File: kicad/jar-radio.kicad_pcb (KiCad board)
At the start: 2 copper layers, 84 x 84 mm, 68 parts, among them J1 USB-C 5V, J2 BATT PH2.0, J3 ANT wire, J4 SPEAKER, Q1 AO3401A, U1 Si4825-A10, U2 NS8002, U3 TP4056, U4 XC6206P332MR, U5 XC61CN2702MR, U6 XB8089D, Y1 32.768kHz

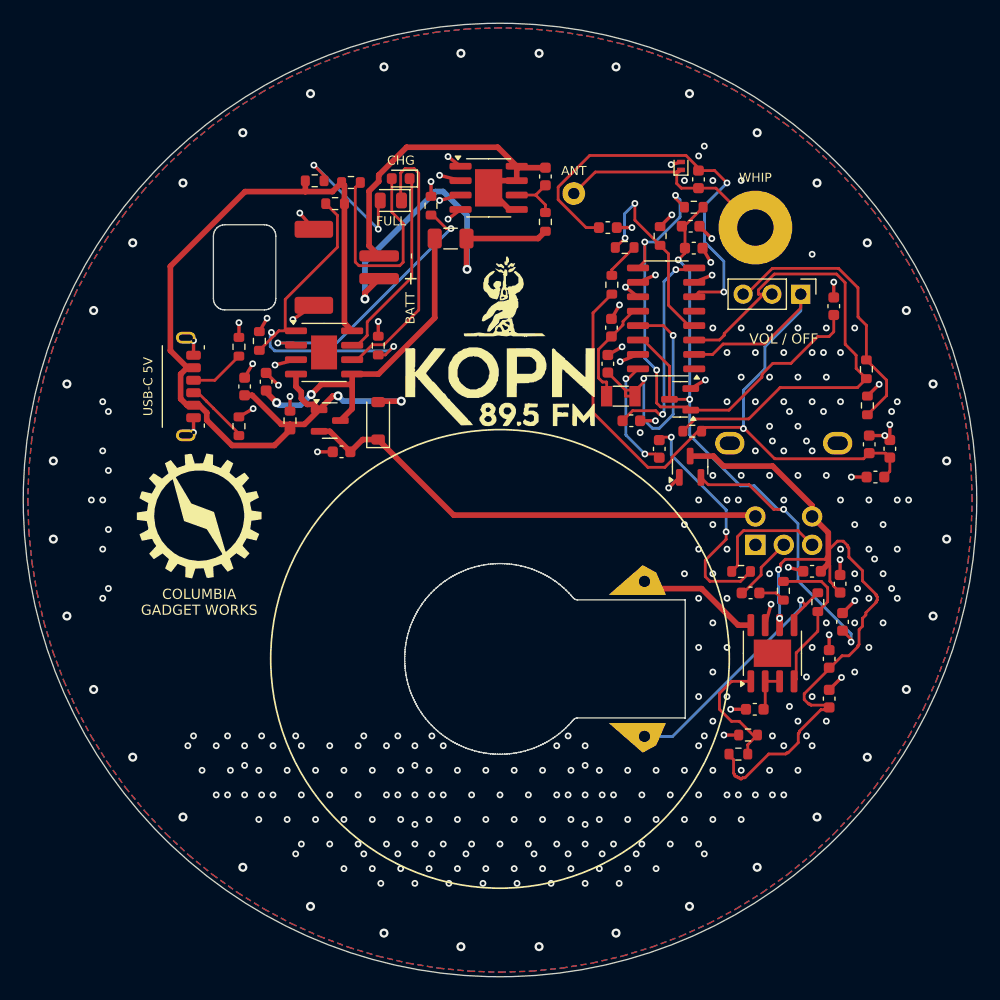
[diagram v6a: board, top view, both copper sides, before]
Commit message: Route with polarity jumpers, moved antenna hole and speaker labels (0 unconnected); exports, renders, BOM check and plan regenerated
Co-Authored-By: Claude Opus 5.5 <noreply@anthropic.com>
Claude-Session: https://claude.ai/code/session_01UChZ4MGw6SzykNSB399iC4
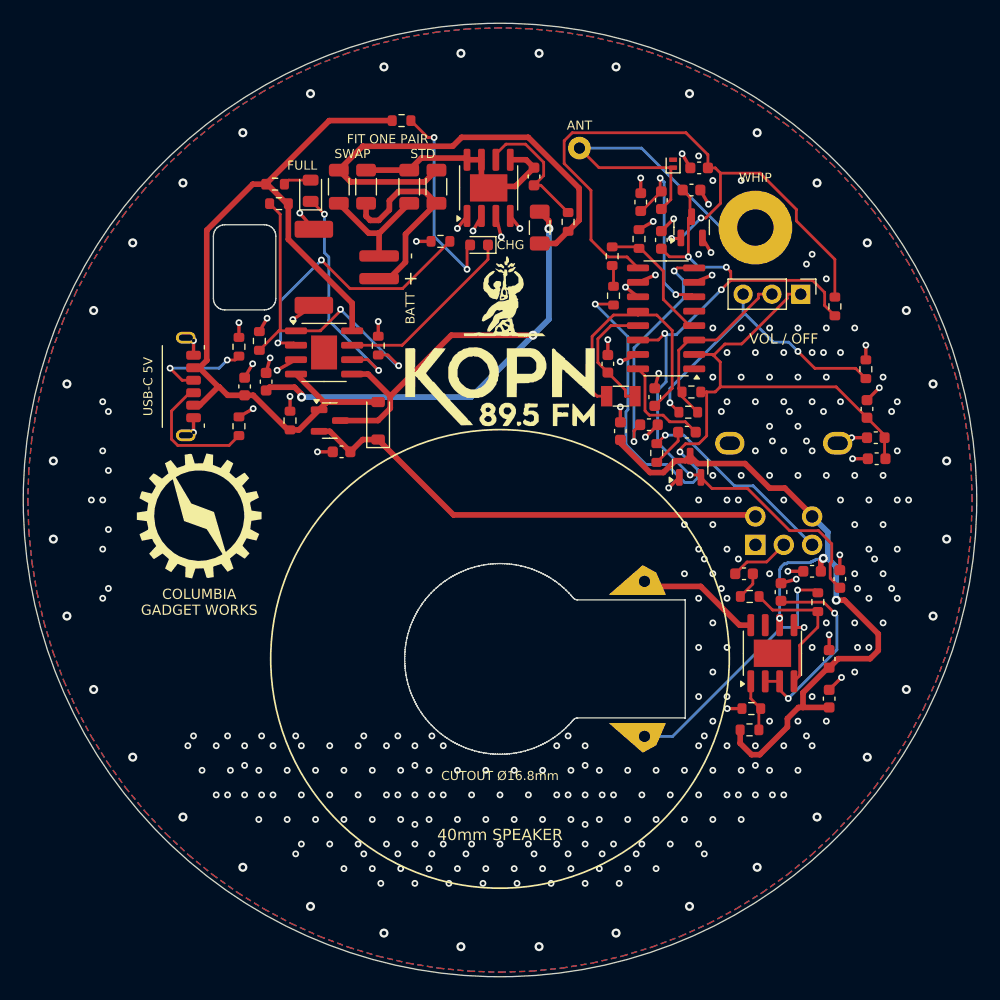
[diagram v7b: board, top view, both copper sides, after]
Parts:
- added R23: 0R (pin1 = -), Resistor_SMD:R_1206_3216Metric, F.Cu at (142.0, 72.4)
- added R24: 0R (pin2 = +), Resistor_SMD:R_1206_3216Metric, F.Cu at (144.4, 72.4)
- added R25: 0R (DNP, pin1 = +), Resistor_SMD:R_1206_3216Metric, F.Cu at (135.8, 72.4)
- added R26: 0R (DNP, pin2 = -), Resistor_SMD:R_1206_3216Metric, F.Cu at (138.2, 72.4)
- moved C19 23.6 mm to (160.6, 93.9)
- moved C5 17.0 mm to (167.5, 70.7), turned to 180 degrees
- moved R3 16.1 mm to (166.6, 92.3), turned to 180 degrees
- moved R1 15.2 mm to (179.5, 82.9), turned to 90 degrees
- moved U5 15.2 mm to (166.9, 76.0), turned to 90 degrees
- moved R22 12.8 mm to (163.8, 95.9), turned to 90 degrees
- moved C12 10.6 mm to (174.8, 108.1), turned to 90 degrees
- moved D2 9.05 mm to (148.2, 77.5)
- moved F1 7.91 mm to (153.5, 76.0), turned to 90 degrees
- moved C2 7.21 mm to (163.6, 90.9)
- moved D3 7.12 mm to (133.3, 72.8), turned to 90 degrees
- moved R14 7.04 mm to (141.3, 66.6)
- moved R20 4.94 mm to (130.5, 73.9)
- moved J3 4.03 mm to (157.0, 69.0)
- moved C20 3.79 mm to (179.9, 107.0)
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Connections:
- J2 pad 1: BAT_N -> BATJ1
- J2 pad 2: BAT_P -> BATJ2
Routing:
- net VBAT: track 29.8 -> 63.1 mm, vias 2 -> 3
- net TUNE2: track 45.4 -> 16.6 mm
- net FMI: track 36.8 -> 16.3 mm
- net BATJ2: track 0.00 -> 18.7 mm
- net AOUT_C: track 20.7 -> 3.44 mm, vias 2 -> 0
- net AMP_BYP: track 3.79 -> 17.6 mm, vias 0 -> 2
- net XTALO: track 9.68 -> 22.3 mm
- net RST: track 45.0 -> 57.3 mm, vias 3 -> 2
- net XTALI: track 23.3 -> 10.9 mm, vias 2 -> 0
- net ANT: track 19.9 -> 31.4 mm
- net BAT_N: track 31.5 -> 20.5 mm
- net BATJ1: track 0.00 -> 10.4 mm
- net LEDG_A: track 12.4 -> 2.46 mm, vias 2 -> 0
- net BAT_P: track 32.7 -> 40.8 mm, vias 2 -> 0
- net VOL_TOP: track 10.6 -> 18.0 mm, vias 0 -> 1
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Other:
- board text added: "40mm SPEAKER"
- board text added: "CUTOUT Ø16.8mm"
- board text added: "FIT ONE PAIR"
- board text added: "STD"
- board text added: "SWAP"

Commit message: Route with the KOPN circle logo (0 unconnected); socket BATT label dropped (overlapped the logo ring); exports, renders, BOM check and plan regenerated
Co-Authored-By: Claude Opus 5.5 <noreply@anthropic.com>
Claude-Session: https://claude.ai/code/session_01UChZ4MGw6SzykNSB399iC4
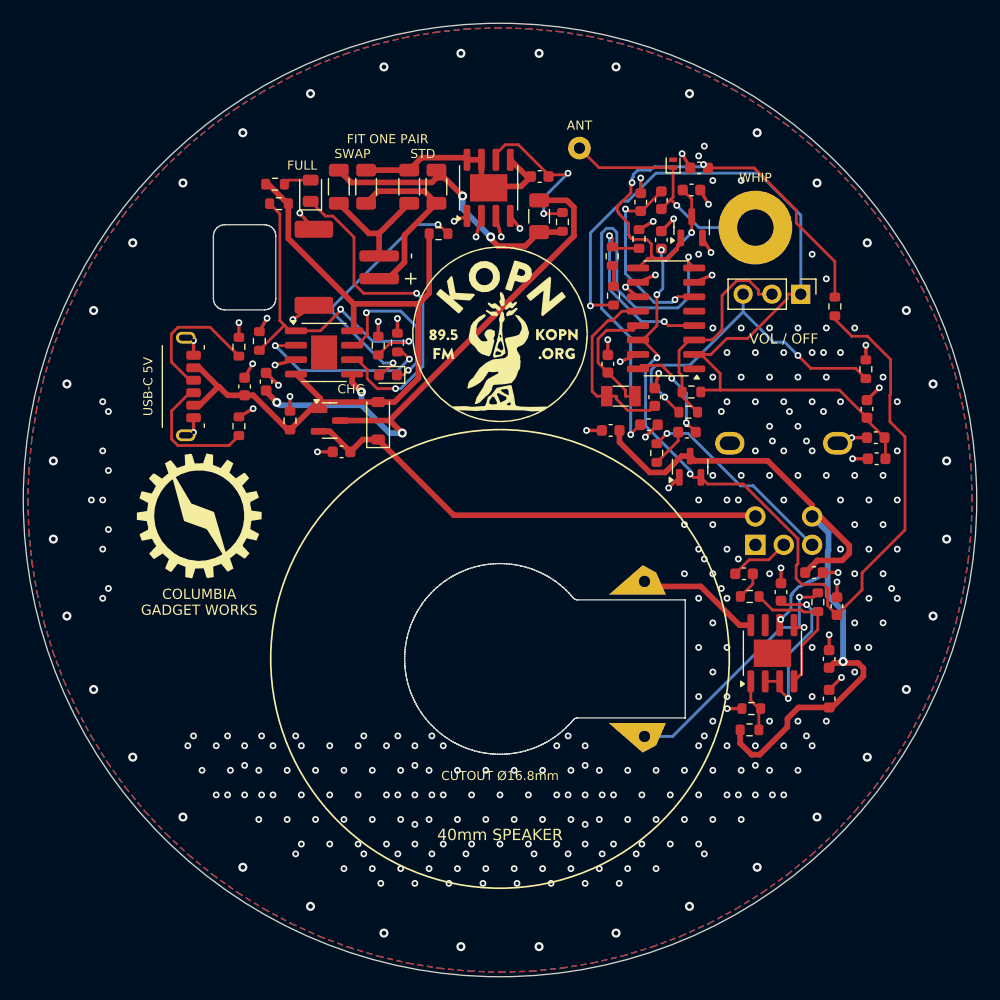
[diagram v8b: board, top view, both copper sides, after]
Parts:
- MK2: value Logo_KOPN_15mm -> Logo_KOPN_Circle_15.5mm; footprint jar-radio:Logo_KOPN_15mm -> jar-radio:Logo_KOPN_Circle_15.5mm
- moved C18 21.7 mm to (159.8, 93.9)
- moved C19 21.1 mm to (177.7, 106.4), turned to 0 degrees
- moved D2 14.0 mm to (140.1, 89.0)
- moved R14 10.5 mm to (144.6, 76.5)
- moved R13 9.69 mm to (141.0, 86.1), turned to 90 degrees
- moved C20 2.40 mm to (179.7, 109.3)
- moved F1 1.00 mm to (153.4, 75.0)
- moved MK2 0.60 mm to (150.0, 85.4)
- moved C22 0.50 mm to (153.5, 71.5), turned to 180 degrees
- moved R18 0.50 mm to (155.5, 75.5)
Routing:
- net AMI: track 20.7 -> 38.8 mm
- net BAT_P: track 40.8 -> 24.8 mm, vias 0 -> 2
- net +3V3: track 68.8 -> 84.7 mm
- net RST: track 57.3 -> 44.3 mm
- net VBAT: track 63.1 -> 51.4 mm
- net STDBY: track 20.2 -> 30.3 mm
- net ANT: track 31.4 -> 21.5 mm, vias 0 -> 1
- net VBUS: track 75.6 -> 66.1 mm
- net PROG: track 24.7 -> 16.3 mm
- net XTALO: track 22.3 -> 16.3 mm
- net VSW: track 67.3 -> 72.9 mm, vias 3 -> 2
- net BAND: track 11.6 -> 17.0 mm, vias 0 -> 2
- net TUNE1: track 68.2 -> 73.6 mm, vias 2 -> 1
- net LEDR_A: track 17.7 -> 22.8 mm
- net CC2: track 9.02 -> 12.3 mm, vias 2 -> 0
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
